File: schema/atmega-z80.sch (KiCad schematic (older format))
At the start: 65 parts, among them J1 USB Connector, J2 SPI Connector, Q1 2N2907, Q2 2N2907, U1 Z84C0010PEG, U2 ATmega324A-PU, U3 AS6C4008-55PCN, U4 SN74HC373N, U5 MCP2221AxP, U6 SN74HC00, U7 SN74HC4066, Y1 20MHz

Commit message: schema v0.1 - using multiplexers plus some fixes
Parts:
- removed C7: 0.1uF, symbol Device:C_Small
- removed D?: LED_USB_IO, symbol Device:LED_ALT
- removed R17, R18, R19, R33: 10K, symbol Device:R
- removed R34, R35: 120, symbol Device:R
- removed U7: SN74HC4066, symbol 4xxx_IEEE:4066
- added C13, C5, C6, C9: 0.1uF, symbol Device:C_Small
- added D7: LED_USER, symbol Device:LED_ALT
- added Q3, Q4: NPN_2N4401, symbol Device:Q_NPN_EBC
- added R22, R23: 120, symbol Device:R
- added R24, R26: 100, symbol Device:R
- added R25: 10K, symbol Device:R
- added U5, U6: SN74HC257, symbol 74xx:74LS257
- D1: value LED_USER -> LED_USB_IO
- D2: value LED_Z80_ACTIVE -> LED_CPU_IO
- D3: value LED_PWR -> LED_EXT_MEM
- D5: value LED_EXT_MEM -> LED_PWR
- D6: value LED_CPU_IO -> LED_Z80_ACTIVE
- Q1, Q2: value 2N2907 -> PNP_2N4403
- R27: value 80 -> 10K
- R29: value 100 -> 68
- R30, R32: value 100 -> 10K
- R31: value 10K -> 22
- renumbered C5 to C10, C8 to C11, C9 to C12, C6 to C7, R20 to R17, R21 to R18, R22 to R19, R23 to R20, R24 to R21, U6 to U7, U5 to U8
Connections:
- net labels added: #A15
- wire segments 307 -> 363
- no-connect marks 16 -> 13
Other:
- note added: "BLUE LED (Vf = 3.6 V, If = 30 mA)"
- note added: "GREEN LEDS (Vf = 2 V, If = 25 mA)"
- note added: "YELLOW LEDS (Vf = 2.1 V, If = 30 mA)"
- note removed: "BLUE LED\nVf = 3.6 V\nIf = 30 mA"
- note removed: "GREEN LEDS\nVf = 2 V\nIf = 25 mA"
- note removed: "YELLOW LEDS\nVf = 2.1 V\nIf = 30 mA"
- moved on the sheet: C10, C4, C7, J1, J2, R1, R10, R11, R12, R13, R14, R15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

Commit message: schema v0.2 - reduce the number of resistors
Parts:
- removed Q4: NPN_2N4401, symbol Device:Q_NPN_EBC
- removed R1, R18, R2, R3, R32, R4, R5, R6: 10K, symbol Device:R
- removed R31: 22, symbol Device:R
- added Q4: PNP_2N4403, symbol Device:Q_PNP_EBC
- added R25: 22, symbol Device:R
- renumbered R7 to R1, R16 to R10, R17 to R11, R19 to R12, R20 to R13, R25 to R14, R21 to R15, R22 to R16, R23 to R17, R24 to R18, R25 to R19, R8 to R2, R26 to R20, R27 to R21, R28 to R22, R29 to R23, R30 to R24, R9 to R3, R10 to R4, R11 to R5, R12 to R6, R13 to R7, R14 to R8, R15 to R9
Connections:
- net +5V: now also Q4.1 (E); no longer R11.1, SW_USER.2
- net A14: now also U7.10, U7.9
- net A15: no longer U7.10, U7.9
- net GND: now also D7.1 (K), R11.1, SW_USER.2; no longer R26.2
- net at D7.2 (A): now also R25.1
- net #A15 renamed #A14
- net USER_LED renamed #USER_LED
- new net: Q4.2 (B), R26.2
- new net: Q4.3 (C), R25.2
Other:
- note added: "(A0 … A5: internal\n pull-up in ATMega)"
- note added: "(internal pull-up in ATMega)"
- note added: "(internal pull-up\n in ATMega)"
- moved on the sheet: C13, R1, R10, R2, R3, R4, R5, R6, R7, R8, R9, SW_RESET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

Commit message: minor changes in schema and readme, nothing functional
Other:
- note added: "banking: 0x8000 - 0xbfff\n(A14=0 and A15=1)"
- moved on the sheet: C13, U7C, U7D
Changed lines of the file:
@@
 Text Label 3300 6900 0    50   ~ 0
 #Q
-Text Label 3000 7950 0    50   ~ 0
+Text Label 3200 7950 0    50   ~ 0
 #WAIT_RESET
-Text Label 3000 8100 0    50   ~ 0
+Text Label 3200 8100 0    50   ~ 0
 #WAIT
 Wire Wire Line
 	1450 2700 2400 2700
-Text Label 3000 8550 0    50   ~ 0
+Text Label 3200 8550 0    50   ~ 0
 #INT
-Text Label 3000 8400 0    50   ~ 0
+Text Label 3200 8400 0    50   ~ 0
 #BUSRQ
-Text Label 3000 8250 0    50   ~ 0
+Text Label 3200 8250 0    50   ~ 0
 #BUSACK
 Text Label 3950 7800 0    50   ~ 0
@@
 	-1   0    0    1
 $EndComp
-Text GLabel 12150 8000 0    50   Input ~ 0
+Text GLabel 12000 8000 0    50   Input ~ 0
 GND_TO_USE_ON_THE_BOARD
-Text GLabel 12100 8650 0    50   Input ~ 0
+Text GLabel 11950 8650 0    50   Input ~ 0
 5V_TO_USE_ON_THE_BOARD
 $Comp
@@
 L power:+5V #PWR?
 U 1 1 612DD22B
-P 5250 10700
-F 0 "#PWR?" H 5250 10550 50  0001 C CNN
-F 1 "+5V" H 5250 10900 50  0000 C CNN
-F 2 "" H 5250 10700 50  0001 C CNN
-F 3 "" H 5250 10700 50  0001 C CNN
-	1    5250 10700
+P 5250 10800
+F 0 "#PWR?" H 5250 10650 50  0001 C CNN
+F 1 "+5V" H 5250 11000 50  0000 C CNN
+F 2 "" H 5250 10800 50  0001 C CNN
+F 3 "" H 5250 10800 50  0001 C CNN
+	1    5250 10800
 	1    0    0    1
 $EndComp
-Text Label 5300 10200 0    50   ~ 0
+Text Label 5700 10200 0    50   ~ 0
 #SYS_RESET
 Wire Wire Line
@@
 	3800 4800 4150 4800
 Wire Wire Line
-	12150 8000 12750 8000
-Wire Wire Line
-	12100 8650 12450 8650
+	12000 8000 12750 8000
+Wire Wire Line
+	11950 8650 12450 8650
 Text Notes 13100 9400 2    79   ~ 0
 CONNECTORS
@@
 L Device:C_Small C13
 U 1 1 61427A73
-P 7150 10950
-F 0 "C13" V 7050 11000 50  0000 L CNN
-F 1 "0.1uF" V 7050 10700 50  0000 L CNN
-F 2 "" H 7150 10950 50  0001 C CNN
-F 3 "~" H 7150 10950 50  0001 C CNN
-	1    7150 10950
-	0    -1   -1   0
-$EndComp
-Wire Wire Line
-	7350 10950 7250 10950
+P 5600 10550
+F 0 "C13" H 5650 10650 50  0000 L CNN
+F 1 "0.1uF" H 5650 10450 50  0000 L CNN
+F 2 "" H 5600 10550 50  0001 C CNN
+F 3 "~" H 5600 10550 50  0001 C CNN
+	1    5600 10550
+	1    0    0    -1
+$EndComp
 Wire Wire Line
 	6600 10700 6950 10700
@@
 Connection ~ 5250 10200
 Wire Wire Line
-	6600 10700 6600 10950
-Wire Wire Line
 	7350 10700 7450 10700
-Wire Wire Line
-	7350 10950 7350 10700
-Connection ~ 7350 10700
-Wire Wire Line
-	6600 10950 7050 10950
 Wire Notes Line
 	6400 10800 10100 10800
@@
 Wire Wire Line
 	6600 10700 6600 10200
-Connection ~ 6600 10700
 Text Label 7350 7600 2    50   ~ 0
 #Z80_CLK
@@
 	7950 4600 9100 4600
 Wire Wire Line
-	8200 3500 8250 3500
-Wire Wire Line
-	7550 3400 7600 3400
-Wire Wire Line
-	7550 3150 7550 3400
-Wire Wire Line
-	8250 3150 7550 3150
-Wire Wire Line
-	8250 2850 8250 3150
-Wire Wire Line
-	8200 2850 8250 2850
+	8200 3600 8250 3600
+Wire Wire Line
+	7550 3500 7600 3500
+Wire Wire Line
+	7550 3250 7550 3500
+Wire Wire Line
+	8250 3250 7550 3250
+Wire Wire Line
+	8250 2950 8250 3250
+Wire Wire Line
+	8200 2950 8250 2950
 Wire Wire Line
 	7950 5350 7950 4600
@@
 	0    -1   -1   0
 $EndComp
-Text Label 7550 3250 0    50   ~ 0
+Text Label 7550 3350 0    50   ~ 0
 #A14
 Wire Wire Line
-	7400 3600 7600 3600
+	7400 3700 7600 3700
 Text Label 12200 6650 0    50   ~ 0
 DATA_BUS_8_BIT
-Text GLabel 7950 3950 0    50   Input ~ 0
+Text GLabel 7950 4050 0    50   Input ~ 0
 #EXT_MEM_LED
 $Comp
 L 74xx:74HC00 U7
 U 4 1 612C8DFC
-P 7900 3500
-F 0 "U7" H 7900 3700 50  0000 C CNN
-F 1 "SN74HC00" H 7900 3300 50  0000 C CNN
-F 2 "" H 7900 3500 50  0001 C CNN
-F 3 "http://www.ti.com/lit/gpn/sn74hc00" H 7900 3500 50  0001 C CNN
-	4    7900 3500
-	1    0    0    -1
-$EndComp
-Text Label 7500 3550 2    50   ~ 0
+P 7900 3600
+F 0 "U7" H 7900 3800 50  0000 C CNN
+F 1 "SN74HC00" H 7900 3400 50  0000 C CNN
+F 2 "" H 7900 3600 50  0001 C CNN
+F 3 "http://www.ti.com/lit/gpn/sn74hc00" H 7900 3600 50  0001 C CNN
+	4    7900 3600
+	1    0    0    -1
+$EndComp
+Text Label 7500 3650 2    50   ~ 0
 A15
-Text Label 7550 2850 2    50   ~ 0
+Text Label 7550 2950 2    50   ~ 0
 A14
 Wire Wire Line
+	7600 2950 7600 3050
+Connection ~ 7600 2950
+Wire Wire Line
+	7600 2950 7400 2950
+Wire Wire Line
 	7600 2850 7600 2950
-Connection ~ 7600 2850
-Wire Wire Line
-	7600 2850 7400 2850
-Wire Wire Line
-	7600 2750 7600 2850
 $Comp
 L 74xx:74HC00 U7
 U 3 1 612C6208
-P 7900 2850
-F 0 "U7" H 7900 3050 50  0000 C CNN
-F 1 "SN74HC00" H 7900 2650 50  0000 C CNN
-F 2 "" H 7900 2850 50  0001 C CNN
-F 3 "http://www.ti.com/lit/gpn/sn74hc00" H 7900 2850 50  0001 C CNN
-	3    7900 2850
-	1    0    0    -1
-$EndComp
-Entry Wire Line
-	7300 2750 7400 2850
-Entry Wire Line
-	7300 3500 7400 3600
+P 7900 2950
+F 0 "U7" H 7900 3150 50  0000 C CNN
+F 1 "SN74HC00" H 7900 2750 50  0000 C CNN
+F 2 "" H 7900 2950 50  0001 C CNN
+F 3 "http://www.ti.com/lit/gpn/sn74hc00" H 7900 2950 50  0001 C CNN
+	3    7900 2950
+	1    0    0    -1
+$EndComp
+Entry Wire Line
+	7300 2850 7400 2950
+Entry Wire Line
+	7300 3600 7400 3700
 Entry Wire Line
 	7750 6600 7650 6700
@@
 	9500 4400 9500 4250
 Wire Wire Line
-	7950 3950 8250 3950
-Connection ~ 8250 3950
-Wire Wire Line
-	8250 3950 8250 4150
-Wire Wire Line
-	8250 3500 8250 3950
+	7950 4050 8250 4050
+Connection ~ 8250 4050
+Wire Wire Line
+	8250 4050 8250 4150
+Wire Wire Line
+	8250 3600 8250 4050
 $Comp
 L 74xx:74LS257 U5
@@
 	6600 10200 10600 10200
 Wire Wire Line
-	5250 10200 6600 10200
+	5250 10200 5600 10200
 Connection ~ 8400 9700
 Wire Wire Line
@@
 Text Notes 10050 1550 0    50   ~ 0
 (internal pull-up in ATMega)
+$Comp
+L power:GND #PWR?
+U 1 1 61A0408E
+P 5600 10800
+F 0 "#PWR?" H 5600 10550 50  0001 C CNN
+F 1 "GND" H 5600 10600 50  0000 C CNN
+F 2 "" H 5600 10800 50  0001 C CNN
+F 3 "" H 5600 10800 50  0001 C CNN
+	1    5600 10800
+	-1   0    0    -1
+$EndComp
+Wire Wire Line
+	5600 10450 5600 10200
+Connection ~ 5600 10200
+Wire Wire Line
+	5600 10200 6600 10200
+Wire Wire Line
+	5600 10650 5600 10800
+Wire Wire Line
+	5250 10700 5250 10800
+Text Notes 7350 2650 0    50   ~ 0
+banking: 0x8000 - 0xbfff\n(A14=0 and A15=1)
 Wire Bus Line
 	8550 2100 8550 3250
 Wire Bus Line
-	7300 2100 7300 3500
+	7300 2100 7300 3600
 Wire Bus Line
 	3400 7600 4550 7600

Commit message: added PCB footprints, changed ISP connector
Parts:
- C1, C10, C12, C13, C2, C3, C4, C5, C6, C7, C9: footprint (none) -> Capacitor_SMD:C_1206_3216Metric_Pad1.33x1.80mm_HandSolder
- C11: value 18uF -> 18pF; footprint (none) -> Capacitor_SMD:C_1206_3216Metric_Pad1.33x1.80mm_HandSolder
- D1, D2, D3, D4, D5, D6, D7: footprint (none) -> LED_THT:LED_D3.0mm
- J1: footprint (none) -> atmega-z80:USB_Mini-B_Molex-54819-0519
- J2: footprint (none) -> Connector_PinHeader_2.54mm:PinHeader_2x05_P2.54mm_Vertical; symbol Connector_Generic:Conn_01x06 -> Connector_Generic:Conn_02x05_Odd_Even
- Q1, Q2, Q3, Q4: footprint (none) -> Package_TO_SOT_THT:TO-92
- R1, R10, R11, R12, R13, R14, R15, R16, R17, R18, R19, R2, R20, R21, R22, R23, R24, R25, R26, R3, R4, R5, R6, R7, R8, R9: footprint (none) -> Resistor_SMD:R_1206_3216Metric_Pad1.30x1.75mm_HandSolder
- SW_RESET1: renamed from SW_RESET; footprint (none) -> Button_Switch_THT:SW_PUSH_6mm_H5mm
- SW_USER1: renamed from SW_USER; footprint (none) -> Button_Switch_THT:SW_PUSH_6mm_H5mm
- U1: footprint (none) -> Package_DIP:DIP-40_W15.24mm_Socket
- U2: footprint Package_DIP:DIP-40_W15.24mm -> Package_DIP:DIP-40_W15.24mm_Socket
- U3: footprint Package_DIP:DIP-32_W15.24mm -> Package_DIP:DIP-32_W15.24mm_Socket
- U4: footprint (none) -> Package_DIP:DIP-20_W7.62mm_Socket
- U5, U6: footprint (none) -> Package_DIP:DIP-16_W7.62mm_Socket
- U7: footprint (none) -> Package_DIP:DIP-14_W7.62mm_Socket
- U8: footprint Package_DIP:DIP-14_W7.62mm -> Package_DIP:DIP-14_W7.62mm_Socket
- Y1: footprint (none) -> Crystal:Crystal_HC49-U_Vertical
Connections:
- net 5V_TO_USE_ON_THE_BOARD is gone; now on net +5V: J1.1 (VBUS)
- net GND_TO_USE_ON_THE_BOARD is gone; now on net GND: J1.5 (GND)
- net #SYS_RESET: now also J2.5 (Pin_5)
- net +5V: now also J2.2 (Pin_2); no longer J2.6 (Pin_6)
- net A0: now also U2.35 (PA5)
- net A1: now also U2.34 (PA6); no longer U2.35 (PA5)
- net A15: now also U7.13
- net A2: now also U2.33 (PA7); no longer U2.34 (PA6)
- net A3: now also U2.1 (PB0)
- net A4: now also U2.2 (PB1); no longer U2.1 (PB0)
- net A5: now also U2.3 (PB2); no longer U2.2 (PB1)
- net D0: now also U2.22 (PC0), U3.13 (DQ0)
- net D1: now also U2.23 (PC1), U3.14 (DQ1); no longer U2.22 (PC0)
- net D2: now also U2.24 (PC2), U3.15 (DQ2); no longer U2.23 (PC1)
- net D3: now also U2.25 (PC3), U3.17 (DQ3); no longer U2.24 (PC2)
- net D4: now also U3.18 (DQ4); no longer U1.9 (D5), U2.25 (PC3)
- net D6: now also U2.28 (PC6), U3.20 (DQ6), U4.17 (D6); no longer U2.27 (PC5), U4.14 (D5)
- net D7: now also U2.29 (PC7), U3.21 (DQ7), U4.18 (D7); no longer U2.28 (PC6), U4.17 (D6)
- net GND: now also J1.6 (Shield), J2.10 (Pin_10), J2.4 (Pin_4), J2.6 (Pin_6), J2.8 (Pin_8); no longer J2.5 (Pin_5)
- net SPI_MISO: now also J2.9 (Pin_9); no longer J2.3 (Pin_3)
- net SPI_MOSI: now also J2.1 (Pin_1); no longer J2.2 (Pin_2)
- net SPI_SCK: now also J2.7 (Pin_7); no longer J2.4 (Pin_4)
- net D5: now reaches U3.19 (DQ5)
- net D5: now also U1.9 (D5), U2.27 (PC5), U4.14 (D5)
- net USB_D-: now reaches J1.2 (D-), U8.12 (D-)
- net USB_D+: now reaches J1.3 (D+), U8.13 (D+)
- net #SPI_SS: no longer names the net of U2.5 (PB4)
- net #SPI_SS: no longer J2.1 (Pin_1)

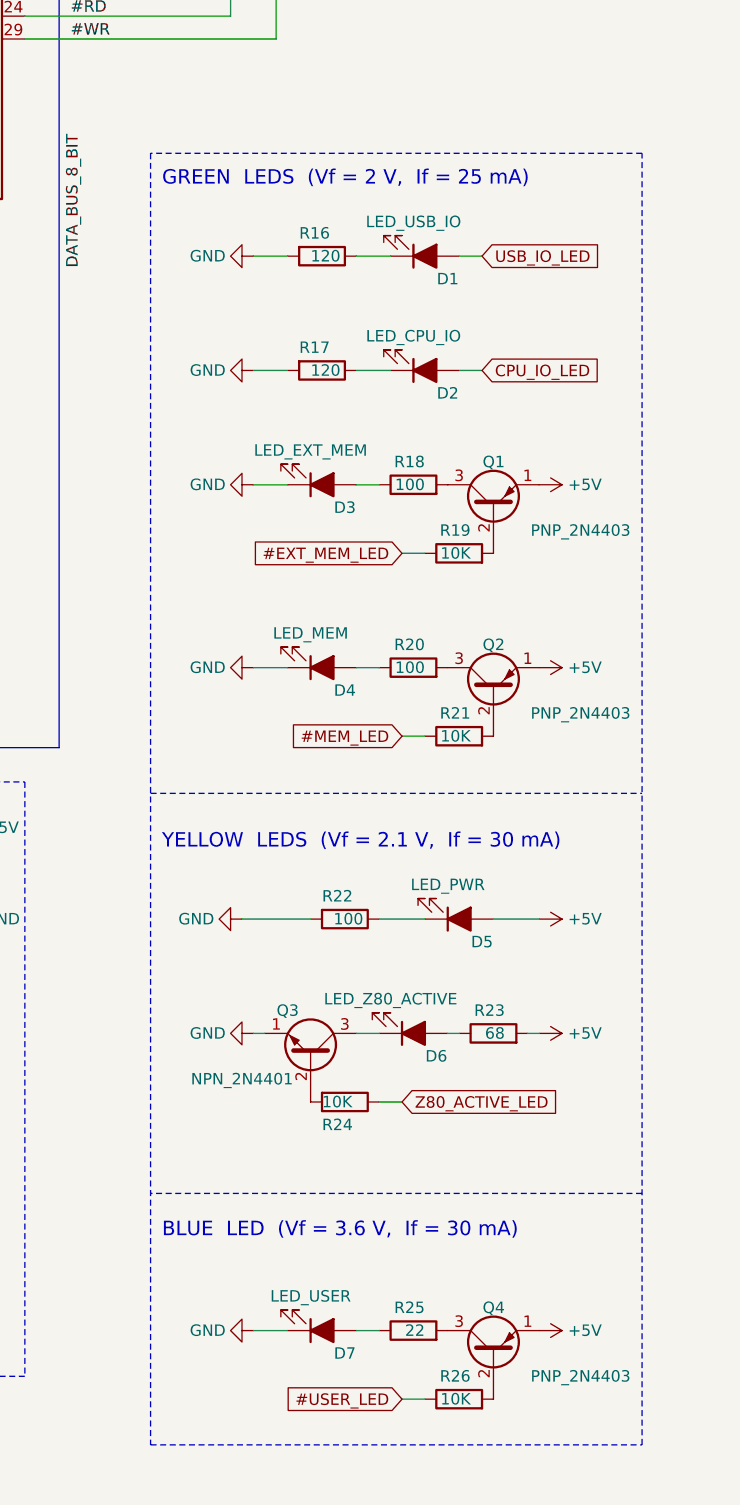
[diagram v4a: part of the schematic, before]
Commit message: update LED resistors
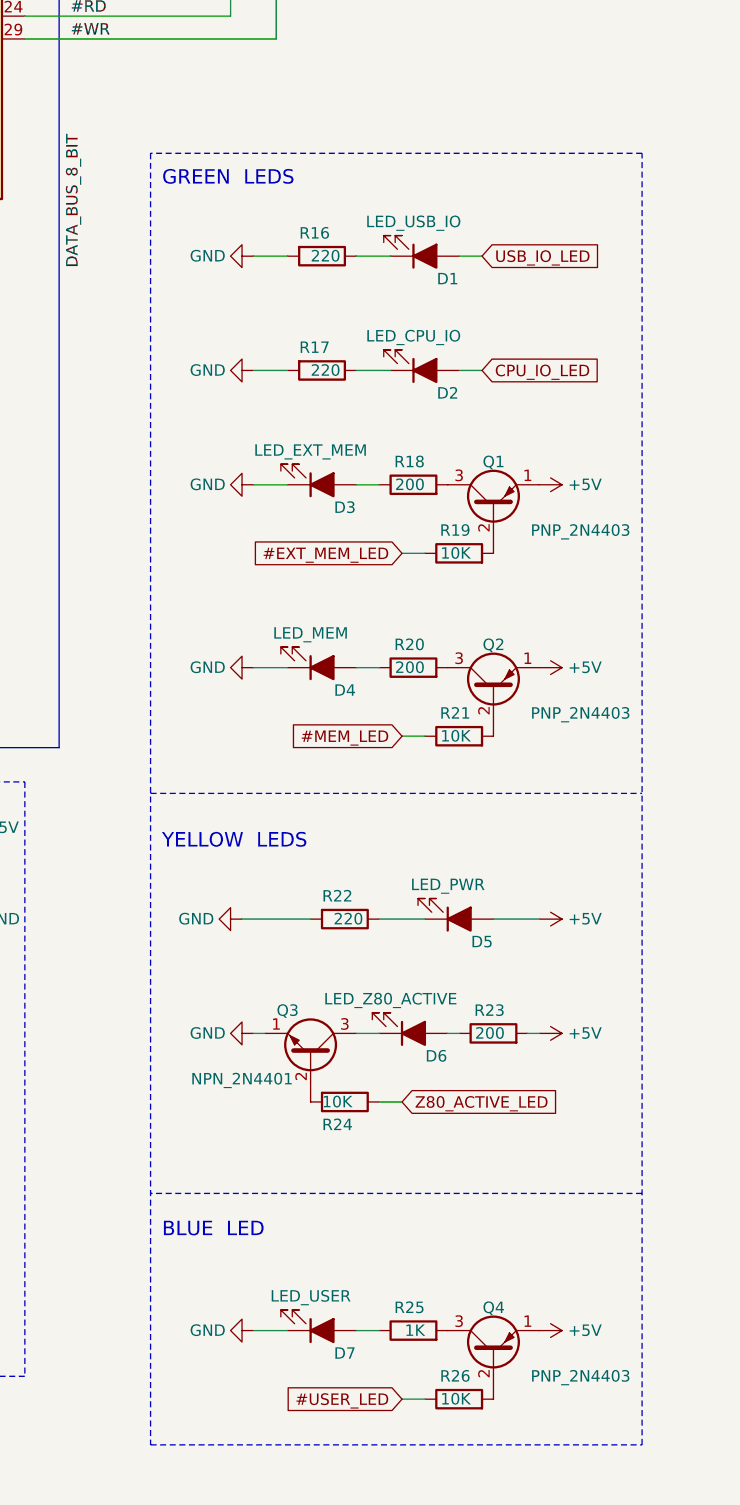
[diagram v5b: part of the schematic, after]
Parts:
- R16, R17: value 120 -> 220
- R18, R20: value 100 -> 200
- R22: value 100 -> 220
- R23: value 68 -> 200
- R25: value 22 -> 1K
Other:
- note added: "BLUE LED"
- note added: "GREEN LEDS"
- note added: "YELLOW LEDS"
- note removed: "BLUE LED (Vf = 3.6 V, If = 30 mA)"
- note removed: "GREEN LEDS (Vf = 2 V, If = 25 mA)"
- note removed: "YELLOW LEDS (Vf = 2.1 V, If = 30 mA)"
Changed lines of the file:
@@
 P 15300 7950
 F 0 "R23" V 15400 7900 50  0000 L CNN
-F 1 "68" V 15300 7900 50  0000 L CNN
+F 1 "200" V 15300 7900 50  0000 L CNN
 F 2 "Resistor_SMD:R_1206_3216Metric_Pad1.30x1.75mm_HandSolder" V 15230 7950 50  0001 C CNN
 F 3 "~" H 15300 7950 50  0001 C CNN
@@
 P 14650 7450
 F 0 "R22" V 14550 7350 50  0000 L CNN
-F 1 "100" V 14650 7400 50  0000 L CNN
+F 1 "220" V 14650 7400 50  0000 L CNN
 F 2 "Resistor_SMD:R_1206_3216Metric_Pad1.30x1.75mm_HandSolder" V 14580 7450 50  0001 C CNN
 F 3 "~" H 14650 7450 50  0001 C CNN
@@
 $EndComp
 Text Notes 13850 7150 0    63   ~ 0
-YELLOW  LEDS  (Vf = 2.1 V,  If = 30 mA)
+YELLOW  LEDS
 Wire Wire Line
 	15150 4550 15250 4550
@@
 P 14550 4550
 F 0 "R16" V 14450 4450 50  0000 L CNN
-F 1 "120" V 14550 4500 50  0000 L CNN
+F 1 "220" V 14550 4500 50  0000 L CNN
 F 2 "Resistor_SMD:R_1206_3216Metric_Pad1.30x1.75mm_HandSolder" V 14480 4550 50  0001 C CNN
 F 3 "~" H 14550 4550 50  0001 C CNN
@@
 P 14550 5050
 F 0 "R17" V 14450 4950 50  0000 L CNN
-F 1 "120" V 14550 5000 50  0000 L CNN
+F 1 "220" V 14550 5000 50  0000 L CNN
 F 2 "Resistor_SMD:R_1206_3216Metric_Pad1.30x1.75mm_HandSolder" V 14480 5050 50  0001 C CNN
 F 3 "~" H 14550 5050 50  0001 C CNN
@@
 $EndComp
 Text Notes 13850 4250 0    63   ~ 0
-GREEN  LEDS  (Vf = 2 V,  If = 25 mA)
+GREEN  LEDS
 Text Notes 13850 8850 0    63   ~ 0
-BLUE  LED  (Vf = 3.6 V,  If = 30 mA)
+BLUE  LED
 Wire Wire Line
 	14400 6350 14250 6350
@@
 P 14950 6350
 F 0 "R20" V 15050 6300 50  0000 L CNN
-F 1 "100" V 14950 6300 50  0000 L CNN
+F 1 "200" V 14950 6300 50  0000 L CNN
 F 2 "Resistor_SMD:R_1206_3216Metric_Pad1.30x1.75mm_HandSolder" V 14880 6350 50  0001 C CNN
 F 3 "~" H 14950 6350 50  0001 C CNN
@@
 P 14950 5550
 F 0 "R18" V 15050 5500 50  0000 L CNN
-F 1 "100" V 14950 5500 50  0000 L CNN
+F 1 "200" V 14950 5500 50  0000 L CNN
 F 2 "Resistor_SMD:R_1206_3216Metric_Pad1.30x1.75mm_HandSolder" V 14880 5550 50  0001 C CNN
 F 3 "~" H 14950 5550 50  0001 C CNN
@@
 P 14950 9250
 F 0 "R25" V 15050 9200 50  0000 L CNN
-F 1 "22" V 14950 9200 50  0000 L CNN
+F 1 "1K" V 14950 9200 50  0000 L CNN
 F 2 "Resistor_SMD:R_1206_3216Metric_Pad1.30x1.75mm_HandSolder" V 14880 9250 50  0001 C CNN
 F 3 "~" H 14950 9250 50  0001 C CNN
@@
 #SYS_RESET
 NoConn ~ 12450 7150
+Wire Wire Line
+	10400 8450 12450 8450
+Wire Wire Line
+	10400 8350 12450 8350
 Wire Bus Line
 	8550 2100 8550 3250
@@
 Wire Bus Line
 	4550 2100 4550 7600
-Wire Wire Line
-	10400 8450 12450 8450
-Wire Wire Line
-	10400 8350 12450 8350
 $EndSCHEMATC

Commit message: adding I2C connector and other fixes
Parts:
- added J3: SPI Connector, symbol Connector_Generic:Conn_01x06
- added J4: I2C Connector, symbol Connector_Generic:Conn_01x04
- added R1, R2: 10K, Resistor_SMD:R_1206_3216Metric_Pad1.30x1.75mm_HandSolder, symbol Device:R
- J2: value SPI Connector -> Programmer ISP 10
- renumbered C11 to C10, C12 to C11, C13 to C12, C9 to C8, C10 to C9, R8 to R10, R9 to R11, R10 to R12, R11 to R13, R12 to R14, R13 to R15, R14 to R16, R15 to R17, R16 to R18, R17 to R19, R18 to R20, R19 to R21, R20 to R22, R21 to R23, R22 to R24, R23 to R25, R24 to R26, R25 to R27, R26 to R28, R1 to R3, R2 to R4, R3 to R5, R4 to R6, R5 to R7, R6 to R8, R7 to R9, SW_RESET1 to SW_RESET, SW_USER1 to SW_USER
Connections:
- net #BUSACK: now also U2.26 (PC4); no longer U2.38 (PA2)
- net #BUSRQ: now also U2.25 (PC3); no longer U2.39 (PA1)
- net #INT: now also U2.24 (PC2); no longer U2.40 (PA0)
- net #R: now also U2.28 (PC6); no longer U2.36 (PA4)
- net #WAIT: now also U2.27 (PC5); no longer U2.37 (PA3)
- net +5V: now also J3.1 (Pin_1), J4.1 (Pin_1)
- net A0: now also U2.1 (PB0); no longer U2.35 (PA5)
- net A1: now also U2.2 (PB1); no longer U2.34 (PA6)
- net A2: now also U2.3 (PB2); no longer U2.33 (PA7)
- net A3: now also U2.4 (PB3); no longer U2.1 (PB0)
- net A4: now also R1.2; no longer U2.2 (PB1)
- net A5: now also R2.2; no longer U2.3 (PB2)
- net CHANGE_BANK_ADDR: now also U2.29 (PC7); no longer U2.4 (PB3)
- net D0: now also U2.40 (PA0); no longer U2.22 (PC0)
- net D1: now also U2.39 (PA1); no longer U2.23 (PC1)
- net D2: now also U2.38 (PA2); no longer U2.24 (PC2)
- net D3: now also U2.37 (PA3); no longer U2.25 (PC3)
- net D4: now also U2.36 (PA4); no longer U2.26 (PC4)
- net D5: now also U2.35 (PA5); no longer U2.27 (PC5)
- net D6: now also U2.34 (PA6); no longer U2.28 (PC6)
- net D7: now also U2.33 (PA7); no longer U2.29 (PC7)
- net GND: now also J3.6 (Pin_6), J4.4 (Pin_4), R1.1, R2.1
- net SPI_MISO: now also J3.5 (Pin_5)
- net SPI_MOSI: now also J3.2 (Pin_2)
- net SPI_SCK: now also J3.4 (Pin_4)
- net #SPI_SS: now reaches U2.5 (PB4)
- net #SPI_SS: now also J3.3 (Pin_3)
- net UART_RXD renamed ATMEGA_RX_AND_USB_TX
- net ATMEGA_RX_AND_USB_TX: now also U8.6 (UTx); no longer U8.5 (URx)
- net UART_TXD renamed ATMEGA_TX_AND_USB_RX
- net ATMEGA_TX_AND_USB_RX: now also U8.5 (URx); no longer U8.6 (UTx)
- new net I2C_SCL: J4.3 (Pin_3), U2.22 (PC0)
- new net I2C_SDA: J4.2 (Pin_2), U2.23 (PC1)
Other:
- note added: "(A0 … A3: internal\n pull-up in ATMega)"
- note removed: "(A0 … A5: internal\n pull-up in ATMega)"
- moved on the sheet: C10, C11, C12, C2, C8, C9, J1, J2, R10, R11, R12, R16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
